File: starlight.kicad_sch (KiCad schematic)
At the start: 14 parts, among them J1 Conn_01x06, U1 AT42QT1012-T

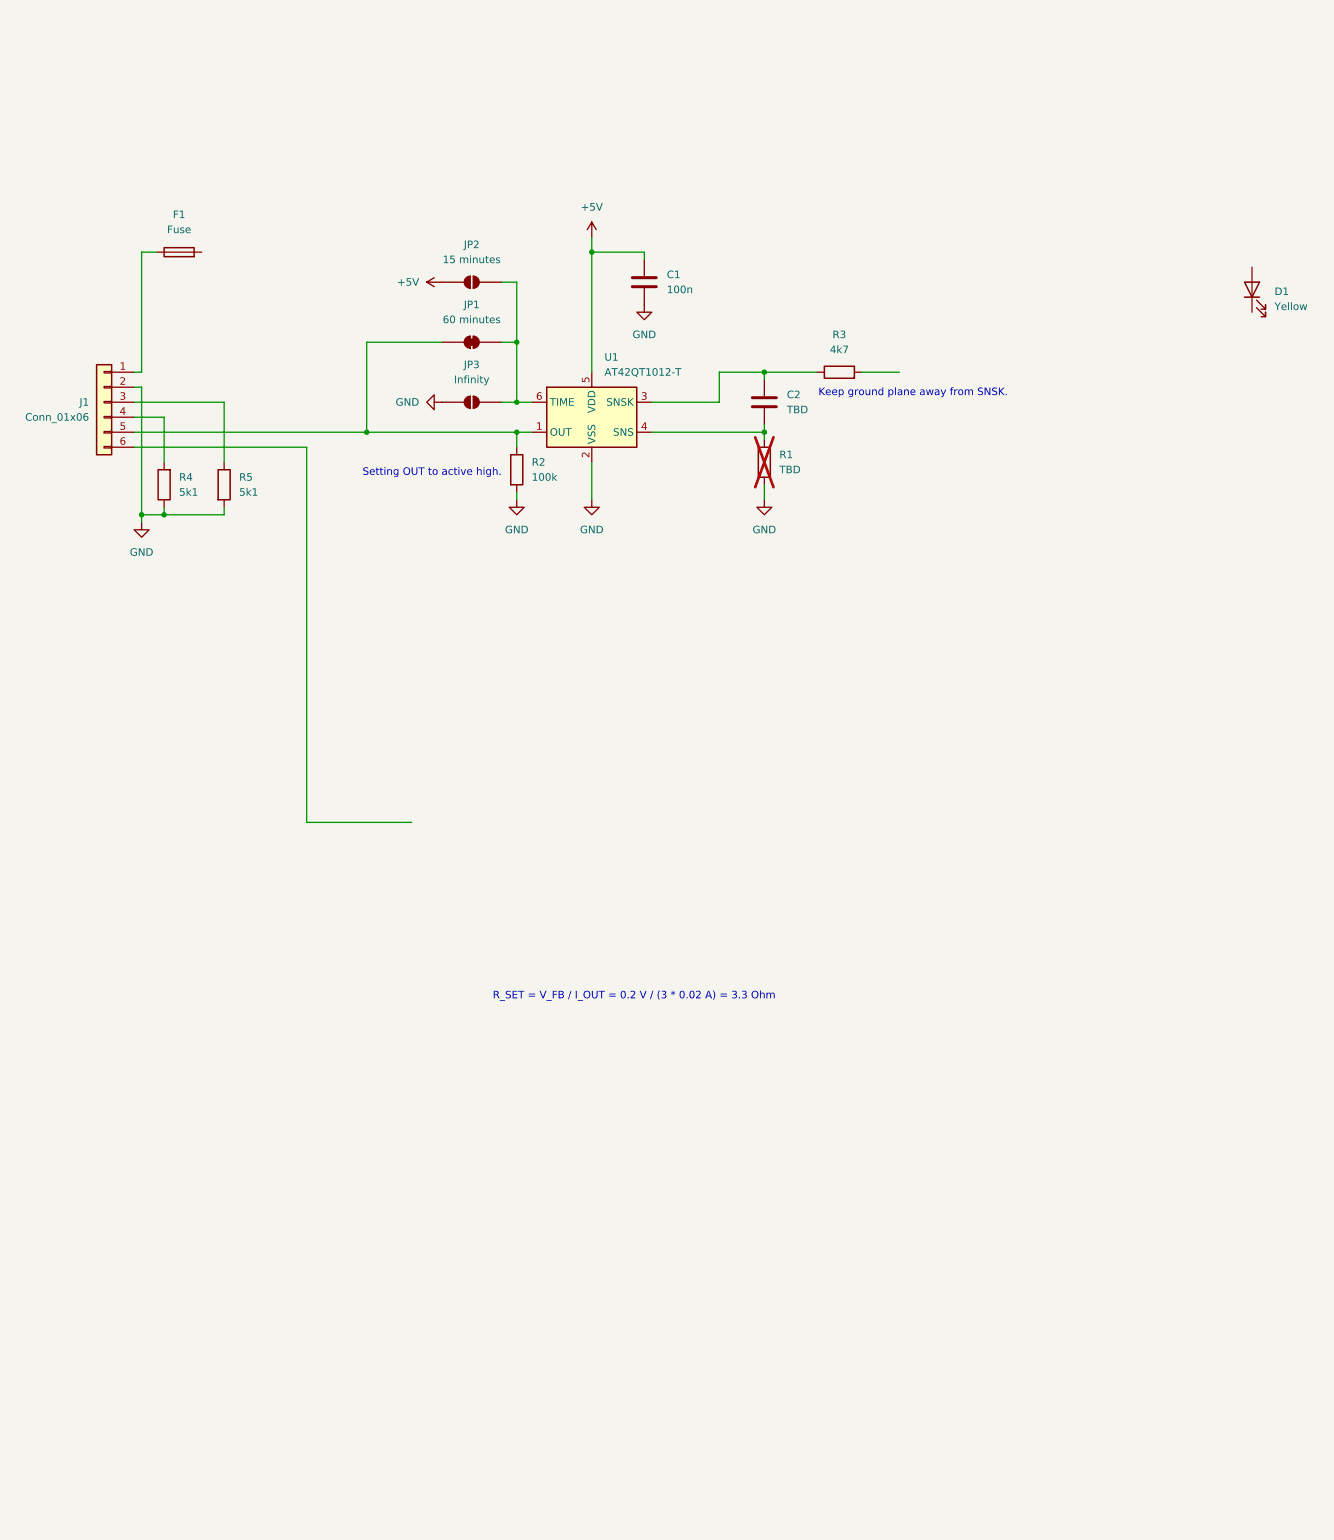
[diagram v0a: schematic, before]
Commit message: Schematic for the LEDs and LED-driver
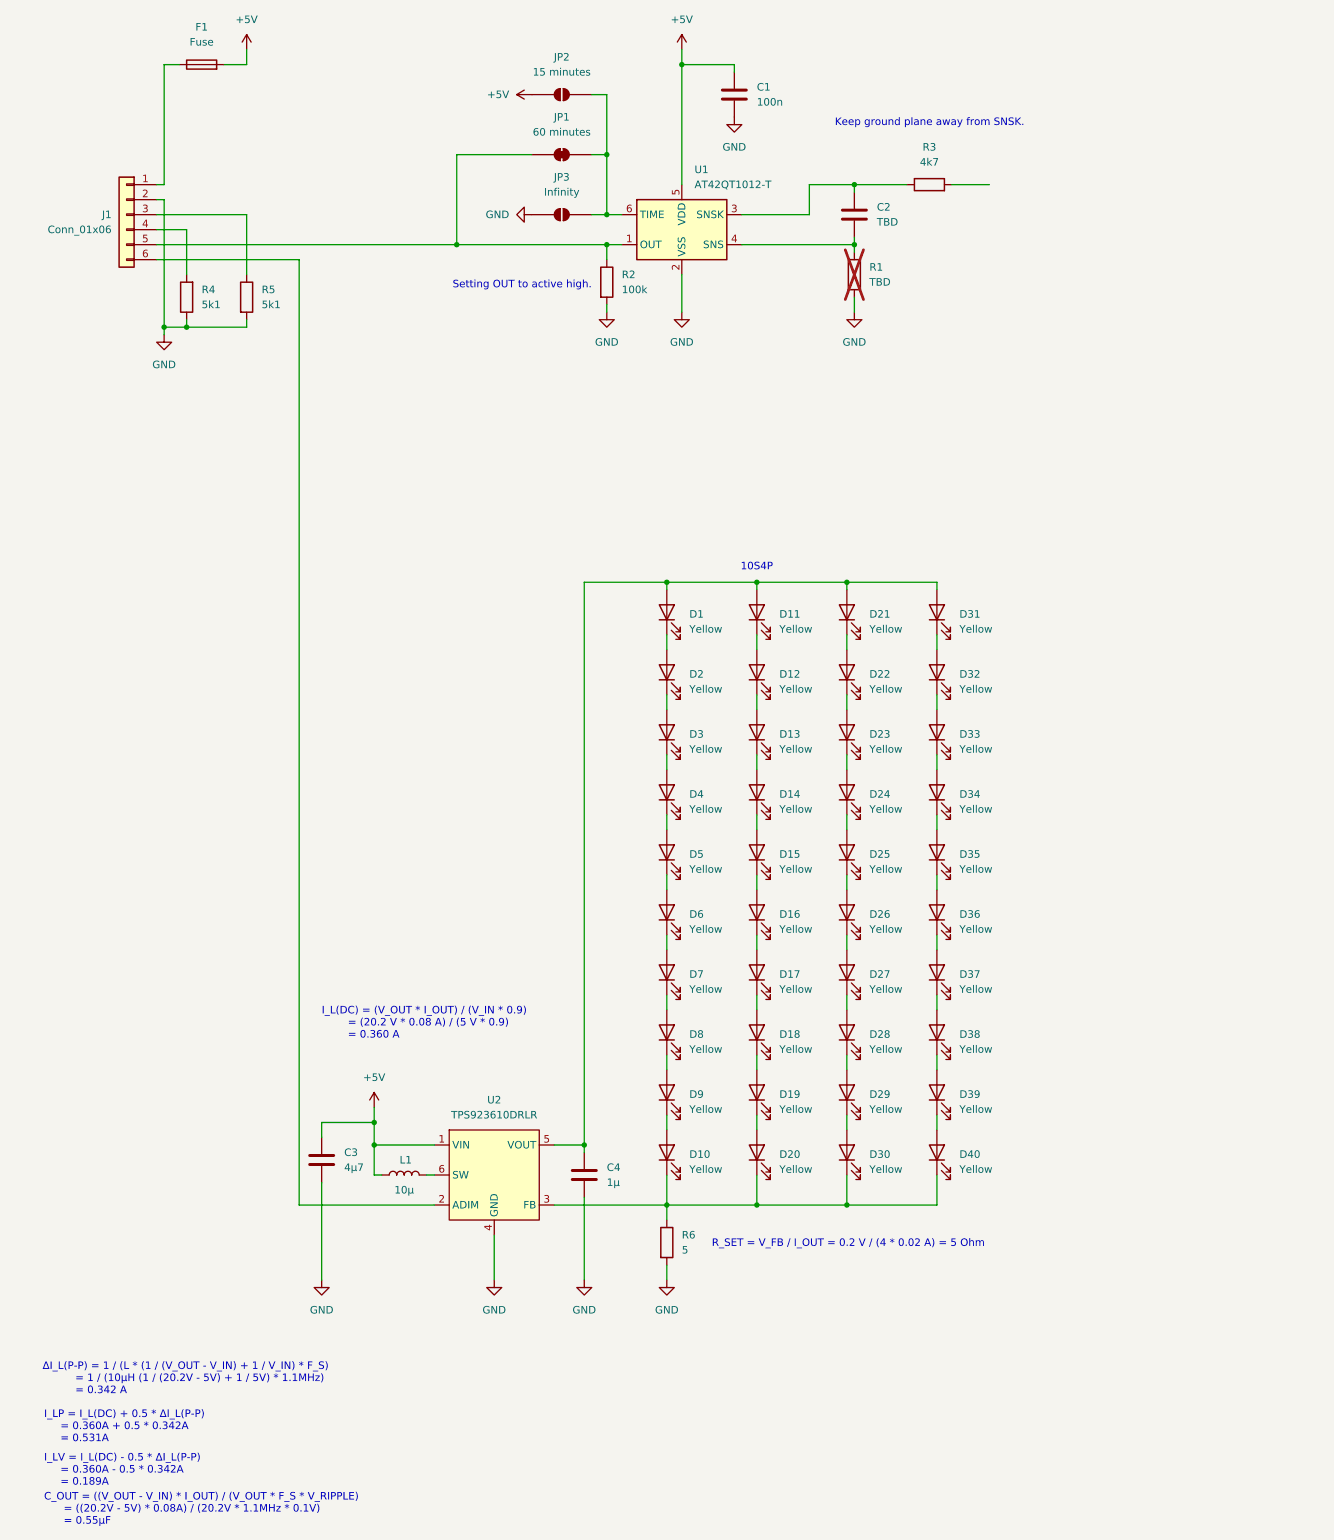
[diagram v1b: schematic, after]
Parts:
- added C3: 4µ7, symbol Device:C
- added C4: 1µ, symbol Device:C
- added D10, D11, D12, D13, D14, D15, D16, D17, D18, D19, D2, D20, D21, D22, D23, D24, D25, D26, D27, D28, D29, D3, D30, D31, D32, D33, D34, D35, D36, D37, D38, D39, D4, D40, D5, D6, D7, D8, D9: Yellow, symbol Device:LED
- added L1: 10µ, symbol Device:L
- added R6: 5, symbol Device:R
- added U2: TPS923610DRLR, Package_TO_SOT_SMD:SOT-563, symbol Starlight:TPS923610
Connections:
- net +5V: now also F1.2, C3.1, L1.1, U2.1 (VIN)
- net GND: now also C3.2, C4.2, R6.2, U2.4 (GND)
- net at D1.1 (K): now also D2.2 (A)
- net at D1.2 (A): now also C4.1, D11.2 (A), D21.2 (A), D31.2 (A), U2.5 (VOUT)
- net at J1.6 (Pin_6): now also U2.2 (ADIM)
- new net: D4.1 (K), D5.2 (A)
- new net: D3.1 (K), D4.2 (A)
- new net: D31.1 (K), D32.2 (A)
- new net: D10.1 (K), D20.1 (K), D30.1 (K), D40.1 (K), R6.1, U2.3 (FB)
- new net: D19.1 (K), D20.2 (A)
- new net: D7.1 (K), D8.2 (A)
- new net: D6.1 (K), D7.2 (A)
- new net: D33.1 (K), D34.2 (A)
- new net: D32.1 (K), D33.2 (A)
- new net: D34.1 (K), D35.2 (A)
- new net: D22.1 (K), D23.2 (A)
- new net: D21.1 (K), D22.2 (A)
- new net: D16.1 (K), D17.2 (A)
- new net: D15.1 (K), D16.2 (A)
- new net: L1.2, U2.6 (SW)
- new net: D8.1 (K), D9.2 (A)
- new net: D5.1 (K), D6.2 (A)
- new net: D39.1 (K), D40.2 (A)
- new net: D2.1 (K), D3.2 (A)
- new net: D25.1 (K), D26.2 (A)
- new net: D24.1 (K), D25.2 (A)
- new net: D14.1 (K), D15.2 (A)
- new net: D13.1 (K), D14.2 (A)
- new net: D29.1 (K), D30.2 (A)
- new net: D10.2 (A), D9.1 (K)
- new net: D28.1 (K), D29.2 (A)
- new net: D17.1 (K), D18.2 (A)
- new net: D37.1 (K), D38.2 (A)
- new net: D36.1 (K), D37.2 (A)
- new net: D11.1 (K), D12.2 (A)
- new net: D35.1 (K), D36.2 (A)
- new net: D12.1 (K), D13.2 (A)
- new net: D38.1 (K), D39.2 (A)
- new net: D23.1 (K), D24.2 (A)
- new net: D26.1 (K), D27.2 (A)
- new net: D27.1 (K), D28.2 (A)
- new net: D18.1 (K), D19.2 (A)
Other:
- note added: "10S4P"
- note added: "C_OUT = ((V_OUT - V_IN) * I_OUT) / (V_OUT * F_S * V_RIPPLE) = ((20.2V - 5V) * 0.08A) / (20.2V * 1.1MHz * 0.1V) = 0.55µF"
- note added: "I_L(DC) = (V_OUT * I_OUT) / (V_IN * 0.9) = (20.2 V * 0.08 A) / (5 V * 0.9) = 0.360 A"
- note added: "I_LP = I_L(DC) + 0.5 * ΔI_L(P-P) = 0.360A + 0.5 * 0.342A = 0.531A"
- note added: "I_LV = I_L(DC) - 0.5 * ΔI_L(P-P) = 0.360A - 0.5 * 0.342A = 0.189A"
- note added: "R_SET = V_FB / I_OUT = 0.2 V / (4 * 0.02 A) = 5 Ohm"
- note added: "ΔI_L(P-P) = 1 / (L * (1 / (V_OUT - V_IN) + 1 / V_IN) * F_S) = 1 / (10µH (1 / (20.2V - 5V) + 1 / 5V) * 1.1MHz) = 0.342 A"
- note removed: "R_SET = V_FB / I_OUT = 0.2 V / (3 * 0.02 A) = 3.3 Ohm"
- moved on the sheet: C1, C2, D1, F1, J1, JP1, JP2, JP3, R1, R2, R3, R4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
